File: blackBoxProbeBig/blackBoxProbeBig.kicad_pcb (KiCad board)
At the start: 4 copper layers, 44 x 44 mm, 84 parts, among them J1 USB-ID, J2 JTAG_2X05, J3 JTAG_2X05, J4 Conn_01x04, Q1 Q_NMOS_DUAL, Q2 Q_PMOS_DUAL, U1 MCP1702-MB, U2 USBLC6-2, U3 STM32F103CBT, U4 74X2T45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

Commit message: small updates
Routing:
- net /USB_V: track 29.0 -> 29.8 mm
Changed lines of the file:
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@@
     (thickness 1.6)
     (drawings 10)
-    (tracks 780)
+    (tracks 784)
     (zones 0)
     (modules 84)
@@
   )
   (setup
-    (last_trace_width 0.127)
+    (last_trace_width 0.2)
     (user_trace_width 0.1524)
     (user_trace_width 0.2)
@@
     (tags SOT-23-6)
     (attr smd)
-    (fp_text reference U2 (at 0 -2.9) (layer F.SilkS)
+    (fp_text reference U2 (at 2.45 -2.45) (layer F.SilkS)
       (effects (font (size 1 1) (thickness 0.15)))
     )
@@
   (via (at 22.7 168.8) (size 0.3556) (drill 0.254) (layers F.Cu B.Cu) (net 36))
   (segment (start 22.7 168.15) (end 22.7 168.7) (width 0.2) (layer F.Cu) (net 36))
-  (segment (start 22.7 168.1) (end 24.3 166.5) (width 0.3) (layer F.Cu) (net 36))
   (segment (start 24.3 166.5) (end 24.3 166.45) (width 0.3) (layer F.Cu) (net 36))
   (segment (start 22.7 168.15) (end 22.7 168.1) (width 0.3) (layer F.Cu) (net 36))
+  (segment (start 22.7 168.15) (end 22.7 167.5) (width 0.2) (layer F.Cu) (net 36))
+  (segment (start 22.7 167.5) (end 22.9 167.3) (width 0.2) (layer F.Cu) (net 36))
+  (segment (start 22.9 167.3) (end 24.1 167.3) (width 0.2) (layer F.Cu) (net 36))
+  (segment (start 24.3 167.1) (end 24.3 166.45) (width 0.2) (layer F.Cu) (net 36))
+  (segment (start 24.1 167.3) (end 24.3 167.1) (width 0.2) (layer F.Cu) (net 36))
   (segment (start 22.81 179.89) (end 22.1 180.6) (width 0.2) (layer F.Cu) (net 37))
   (segment (start 22.1 180.6) (end 21.35 180.6) (width 0.2) (layer F.Cu) (net 37))

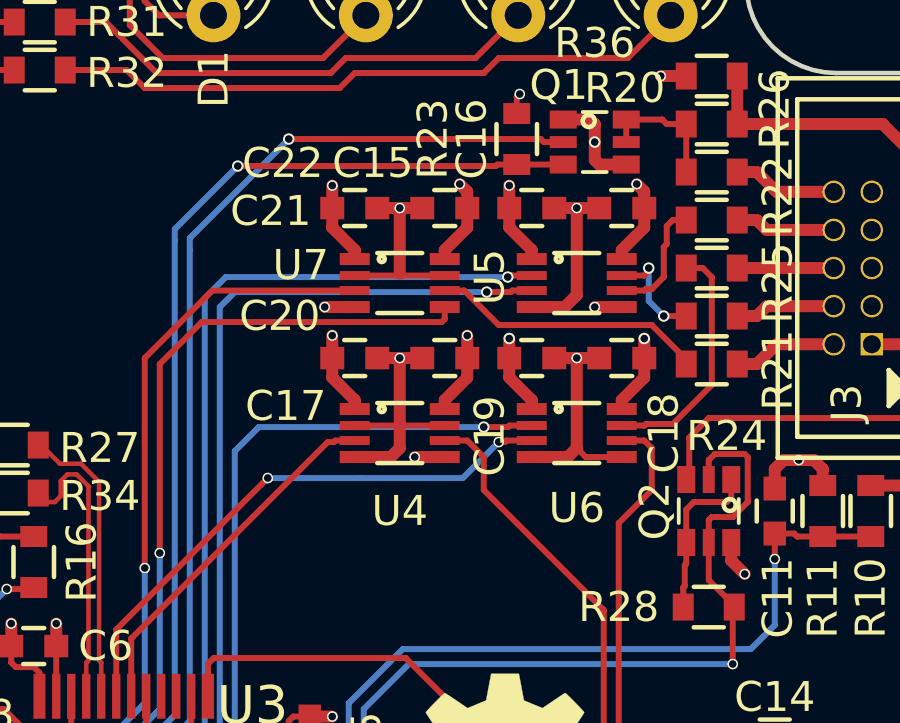
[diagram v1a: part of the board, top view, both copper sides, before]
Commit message: footprint updates
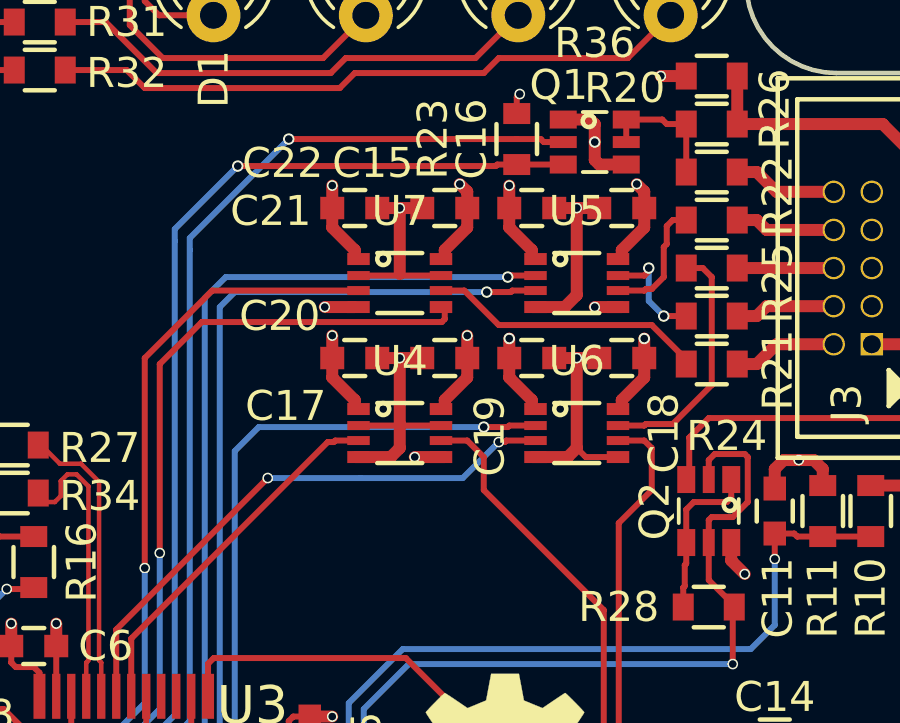
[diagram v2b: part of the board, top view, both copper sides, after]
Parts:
- U4, U5, U6, U7: footprint SquantorIC:NXP_SOT765-1_HAND -> SquantorIC:SOT765-1-NXP
